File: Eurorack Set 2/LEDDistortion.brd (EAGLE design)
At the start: 19 x 106.5 mm, 32 parts, among them IC1 TL072, IC2 TL072

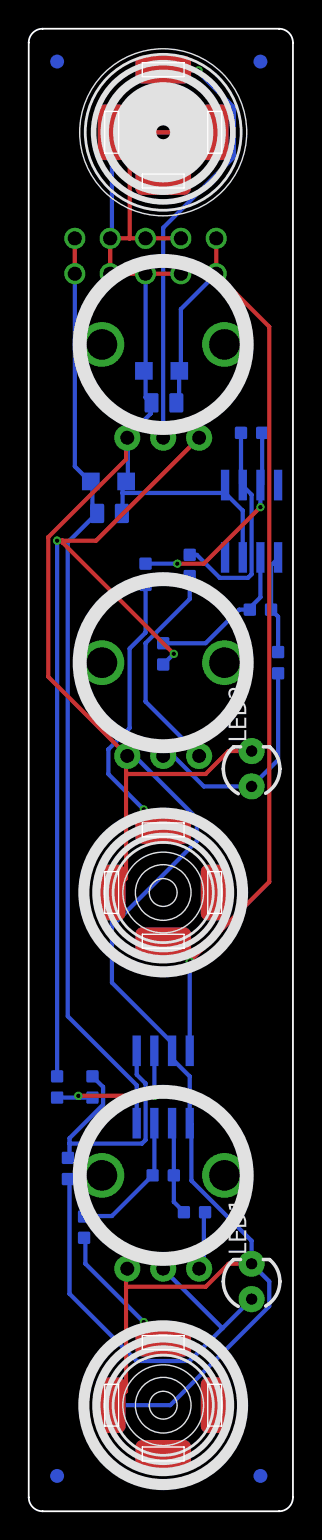
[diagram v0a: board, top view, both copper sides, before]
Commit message: panel dxfs and LEDDistortion updates
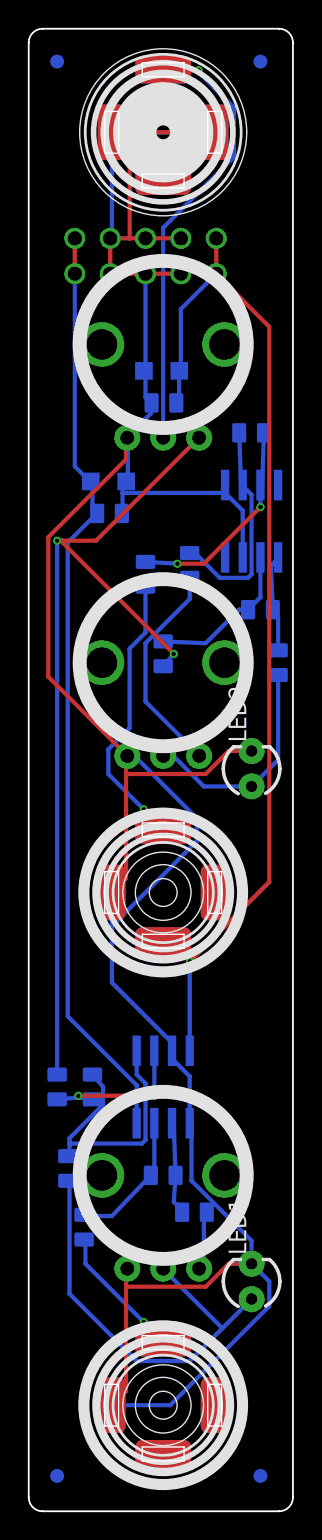
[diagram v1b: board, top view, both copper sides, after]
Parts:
- GAIN1, POST1, POST2: value (none) -> 100k
- R1, R10, R11, R5, R8: device OPL:R0603 -> OPL:C0805
- R12, R3: value (none) -> 100; device OPL:R0603 -> OPL:C0805
- R2, R4, R9: value (none) -> 100k; device OPL:R0603 -> OPL:C0805
- R6, R7: value (none) -> 330; device OPL:R0603 -> OPL:C0805

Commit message: More lauri feedback incorporated
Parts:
- removed R11, R5: (no value), OPL:C0805
- R10: value (none) -> 100k
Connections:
- removed net N$1: POST1.P$3, R5.2
- removed net N$11: POST2.P$3, R11.2
- net N$10: now also POST2.P$3; no longer R11.1
- net N$4: now also POST1.P$3; no longer R5.1
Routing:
- net N$11: track 15.7 -> 0.00 mm
- net N$2: track 31.2 -> 18.5 mm
- net N$10: track 15.8 -> 26.2 mm
- net GND: track 208.3 -> 199.5 mm
- net N$4: track 6.73 -> 11.2 mm
- net N$1: track 4.39 -> 0.00 mm
- net N$3: track 64.2 -> 60.2 mm
- net OP1OUT1: track 7.01 -> 7.54 mm

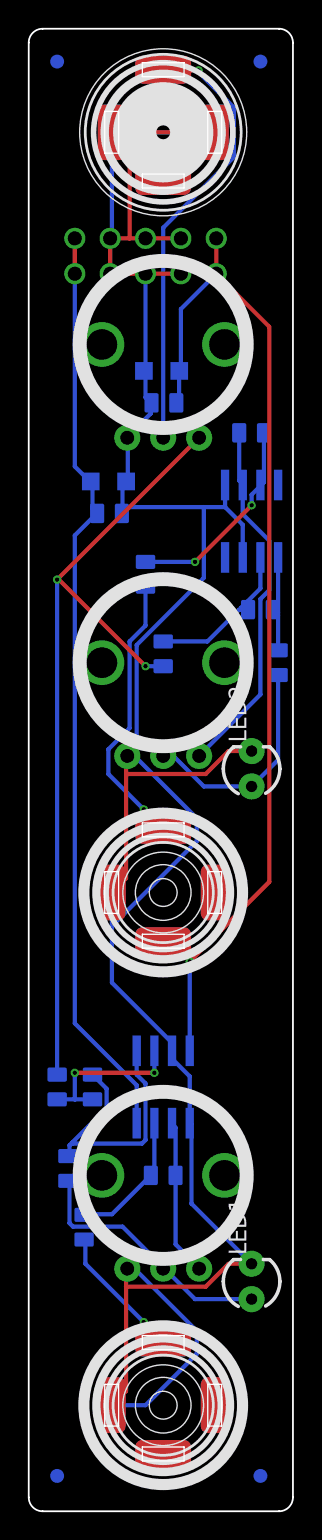
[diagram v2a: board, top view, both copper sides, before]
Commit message: Optional LR Phasor + serial switch jumper on LED distortion
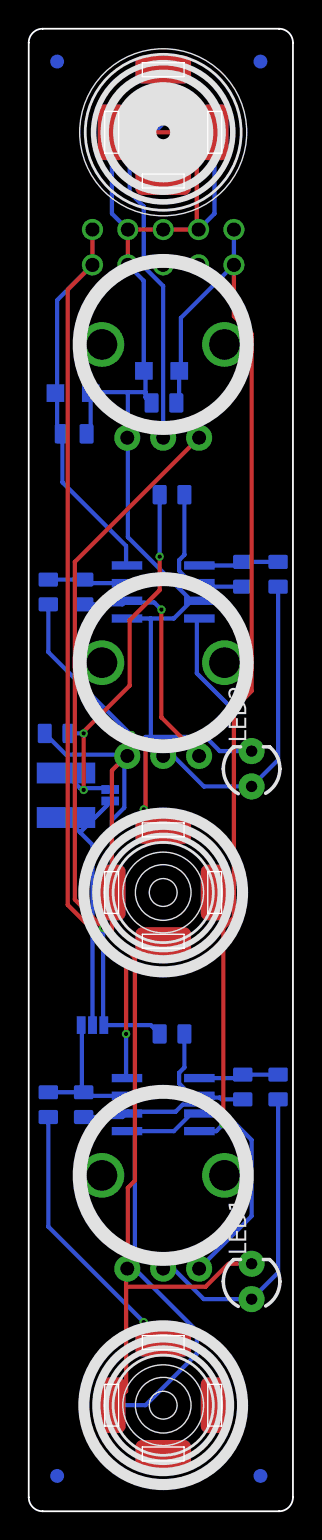
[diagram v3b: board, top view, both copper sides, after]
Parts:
- added L1: TBD, OPL:L0420
- added R5: TBD, OPL:C0805
- added SJ1: (no value), SparkFun-Passives:SJ_3_PASTE1&2
- added SJ2: SOLDERJUMPERNC, SparkFun-Passives:SJ_2S
- C5, C6: value (none) -> 100n
- C7, C8: value (none) -> 10u
- LED1: value (none) -> REDBLUE
- LED2: value (none) -> BLUERED
- R1, R8: value (none) -> TBD
- moved R10 16.6 mm to (4.45, 66.0), turned to 270 degrees
- moved R6 16.2 mm to (18.4, 30.5)
- moved R8 11.4 mm to (10.8, 73.0), turned to 0 degrees
- moved R2 10.8 mm to (15.9, 30.5)
- moved R3 9.17 mm to (1.91, 29.2)
- moved R1 9.09 mm to (10.8, 34.3), turned to 0 degrees
- moved IC2 8.13 mm to (10.2, 66.0), turned to 270 degrees
- moved R4 7.65 mm to (4.45, 29.2), turned to 270 degrees
- moved R12 7.10 mm to (1.91, 66.0)
- moved C7 6.84 mm to (3.69, 80.3)
- moved R7 6.35 mm to (18.4, 67.3)
- moved C5 6.25 mm to (3.76, 77.4)
- moved R9 2.84 mm to (15.9, 67.3), turned to 270 degrees
- moved U$1 1.42 mm to (10.2, 90.8)
- moved IC1 1.27 mm to (10.2, 29.2), turned to 270 degrees
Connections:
- removed net V+: IC2.8
- removed net V-: IC2.4
- new net N$1: L1.2, SJ1.2, SJ2.2
- new net N$8: L1.1, R5.1, R8.2, SJ2.1
- net GND: now also R5.2
- net N$3: now also SJ1.1; no longer R8.2
- net OP2OUT: now also SJ1.3
- net VNEG: now also IC2.4
- net VPOS: now also IC2.8
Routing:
- net N$8: track 0.00 -> 28.4 mm, vias 0 -> 3
- net VPOS: track 66.8 -> 88.4 mm, vias 0 -> 1
- net N$1: track 0.00 -> 18.8 mm
- net VNEG: track 72.8 -> 87.0 mm, vias 1 -> 2
- net OP1OUT: track 19.6 -> 5.76 mm
- net N$4: track 11.2 -> 24.3 mm
- net N$5: track 11.8 -> 21.7 mm
- net GND: track 199.5 -> 208.7 mm
- net N$3: track 60.2 -> 51.0 mm, vias 2 -> 1
- net OP2OUT1: track 14.9 -> 5.76 mm, vias 2 -> 0
- net N$10: track 26.2 -> 17.6 mm, vias 0 -> 1
- net N$7: track 16.1 -> 22.4 mm
- net N$6: track 34.7 -> 30.0 mm
- net N$2: track 18.5 -> 22.4 mm
- net OP1NEG: track 11.7 -> 8.78 mm, vias 2 -> 0
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
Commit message: Full configurable LRC stage on the LEDDistortion - placement cleanup
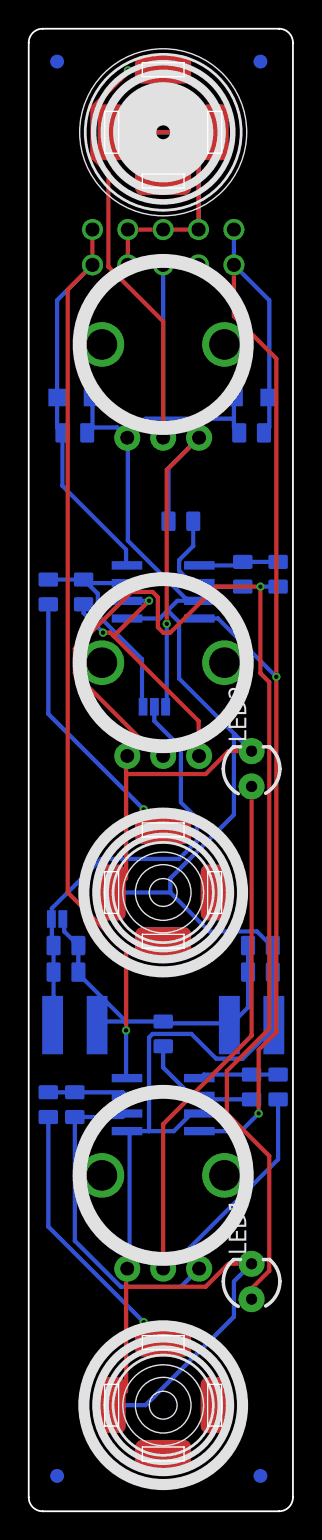
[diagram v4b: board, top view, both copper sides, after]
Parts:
- added C1, C2: 100n, OPL:C0805
- added L2: TBD, OPL:L0420
- added R11: TBD, OPL:C0805
- moved R8 38.7 mm to (10.2, 34.3), turned to 90 degrees
- moved R1 36.8 mm to (11.4, 71.1)
- moved R10 36.8 mm to (3.81, 29.2)
- moved R9 36.8 mm to (16.5, 30.5)
- moved IC1 36.8 mm to (10.2, 66.0)
- moved IC2 36.8 mm to (10.2, 29.2)
- moved R12 36.8 mm to (1.91, 29.2)
- moved R3 36.8 mm to (1.91, 66.0)
- moved R4 36.8 mm to (4.45, 66.0)
- moved U$3 36.8 mm to (10.2, 44.5)
- moved U$6 36.8 mm to (10.2, 7.62)
- moved POST1 36.8 mm to (10.2, 61.0)
- moved POST2 36.8 mm to (10.2, 24.1)
- moved R2 36.8 mm to (15.9, 67.3)
- moved R6 36.8 mm to (18.4, 67.3)
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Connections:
- net GND: now also C1.2, L2.2
- net N$1: now also C2.1, R11.1
- net N$8: now also C1.1, C2.2, L2.1, R11.2
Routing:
- net N$2: track 22.4 -> 85.3 mm, vias 0 -> 1
- net N$7: track 22.4 -> 53.1 mm
- net N$3: track 51.0 -> 27.3 mm
- net GND: track 208.7 -> 223.0 mm
- net N$1: track 18.8 -> 31.9 mm
- net OP2OUT: track 10.7 -> 16.7 mm
- net N$10: track 17.6 -> 23.6 mm, vias 1 -> 0
- net N$6: track 30.0 -> 34.7 mm
- net N$4: track 24.3 -> 19.8 mm, vias 0 -> 2
- net VNEG: track 87.0 -> 90.6 mm
- net N$8: track 28.4 -> 25.4 mm, vias 3 -> 0
- net OP1NEG1: track 10.7 -> 8.84 mm
- net N$12: track 21.8 -> 21.7 mm, vias 2 -> 1

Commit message: New DXFs, triple LRC stage for LEDDist
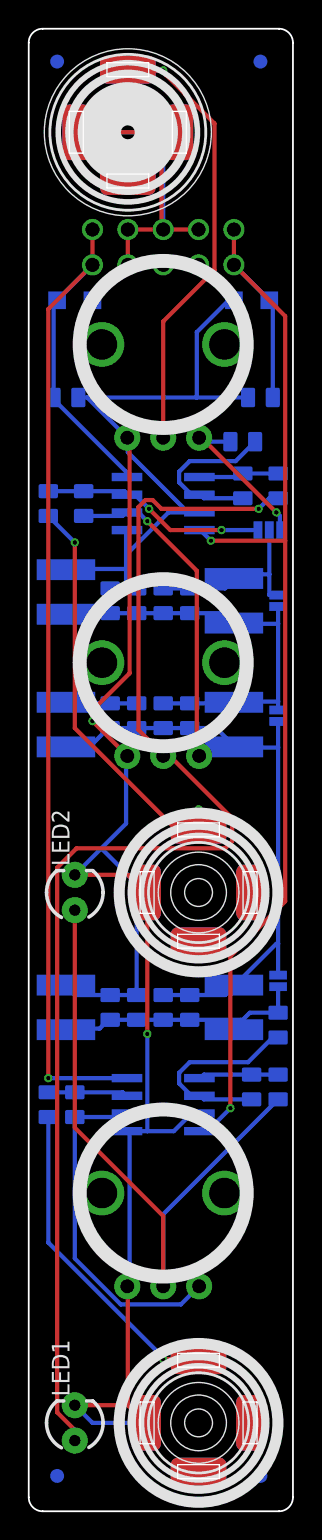
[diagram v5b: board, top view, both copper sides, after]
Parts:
- added C10, C3, C4, C9: 100n, OPL:C0805
- added L3, L4, L5, L6: TBD, OPL:L0420
- added R13, R14, R15, R16: TBD, OPL:C0805
- added SJ3, SJ4: SOLDERJUMPERNC, SparkFun-Passives:SJ_2S
- moved L2 33.9 mm to (3.17, 66.0), turned to 90 degrees
- moved L1 32.6 mm to (15.2, 65.4), turned to 90 degrees
- moved C1 28.1 mm to (8.26, 65.4), turned to 90 degrees
- moved SJ2 27.8 mm to (18.4, 65.4), turned to 90 degrees
- moved C2 27.6 mm to (10.2, 65.4), turned to 270 degrees
- moved R5 27.0 mm to (6.35, 65.4), turned to 90 degrees
- moved R11 26.3 mm to (12.1, 65.4), turned to 270 degrees
- moved LED1 16.3 mm to (3.81, 6.35)
- moved LED2 15.5 mm to (3.81, 44.5)
- moved SJ1 15.1 mm to (17.8, 70.5)
- moved R8 8.28 mm to (18.4, 34.9)
- moved R1 7.24 mm to (15.9, 76.8)
- moved C7 6.98 mm to (3.81, 87.0)
- moved C8 6.98 mm to (16.5, 87.0)
- moved IC1 6.35 mm to (10.2, 72.4)
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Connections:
- removed net N$8: C1.1, C2.2, L1.1, L2.1, R11.2, R5.1, R8.2, SJ2.1
- new net N$11: C1.1, C2.2, C4.1, L1.1, L2.1, L3.2, R11.2, R14.1, R5.1, SJ2.1, SJ3.2
- new net N$13: C10.2, C9.1, L5.1, L6.1, R15.1, R16.2, R8.2, SJ4.1
- new net N$14: C10.1, C3.1, C4.2, L3.1, L4.1, L5.2, R13.1, R14.2, R16.1, SJ3.1, SJ4.2
- net GND: now also C3.2, C9.2, L4.2, L6.2, R13.2, R15.2
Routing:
- net N$14: track 0.00 -> 44.5 mm
- net N$11: track 0.00 -> 31.4 mm
- net N$8: track 25.4 -> 0.00 mm
- net N$13: track 0.00 -> 19.4 mm
- net N$1: track 31.9 -> 13.4 mm
- net N$3: track 27.3 -> 11.6 mm
- net N$5: track 21.7 -> 30.9 mm, vias 1 -> 2
- net N$2: track 85.3 -> 92.9 mm
- net N$7: track 53.1 -> 46.5 mm
- net OP1NEG1: track 8.84 -> 14.6 mm
- net N$12: track 21.7 -> 26.1 mm
- net VNEG: track 90.6 -> 86.3 mm
- net N$4: track 19.8 -> 23.4 mm, vias 2 -> 1
- net OP1NEG: track 9.05 -> 12.2 mm
- net GND: track 223.0 -> 220.4 mm, vias 0 -> 2
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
